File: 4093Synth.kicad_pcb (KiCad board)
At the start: 2 copper layers, 13 parts, among them U1 HEF4093B

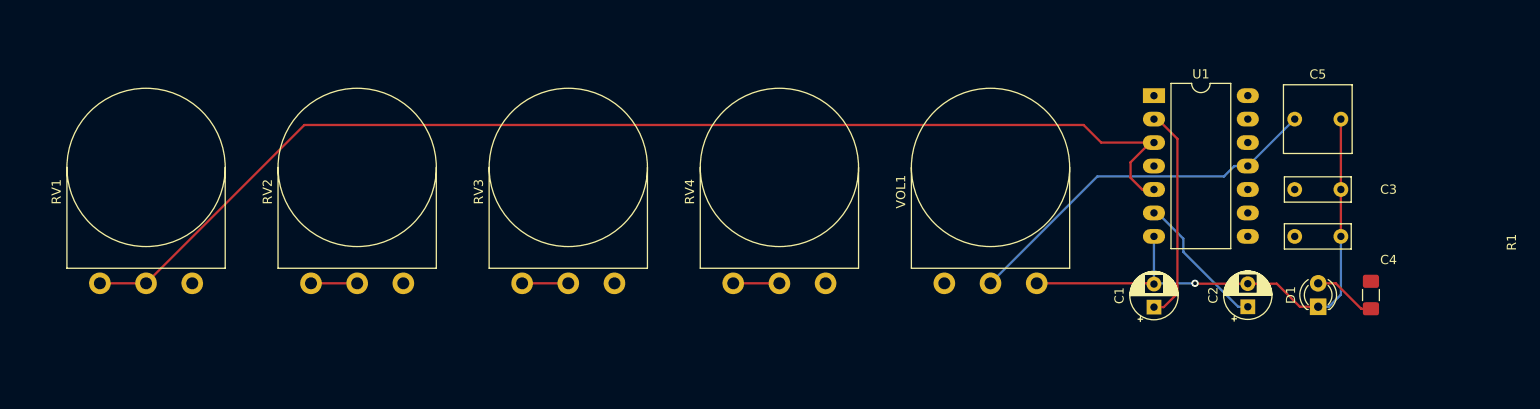
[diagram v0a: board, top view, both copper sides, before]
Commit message: Adds CV in for each Pot
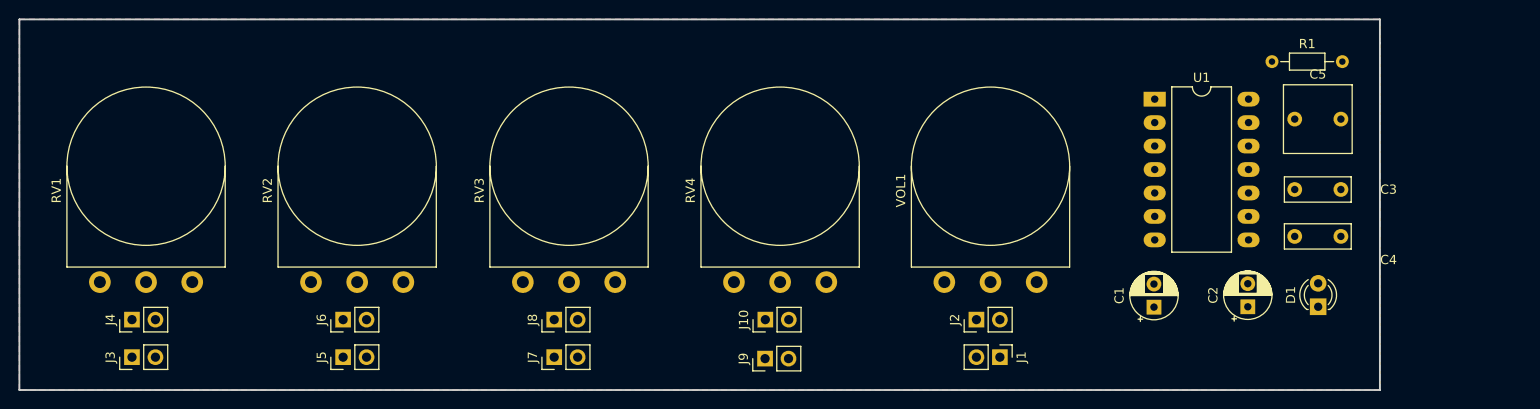
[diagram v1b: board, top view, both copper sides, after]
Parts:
- added J1: Conn_01x02_Female, Connector_PinHeader_2.54mm:PinHeader_1x02_P2.54mm_Vertical, F.Cu at (156.0, 117.2)
- added J10: Conn_01x02_Female, Connector_PinHeader_2.54mm:PinHeader_1x02_P2.54mm_Vertical, F.Cu at (130.6, 113.2)
- added J2: Conn_01x02_Female, Connector_PinHeader_2.54mm:PinHeader_1x02_P2.54mm_Vertical, F.Cu at (153.5, 113.2)
- added J3: Conn_01x02_Female, Connector_PinHeader_2.54mm:PinHeader_1x02_P2.54mm_Vertical, F.Cu at (62.1, 117.2)
- added J4: Conn_01x02_Female, Connector_PinHeader_2.54mm:PinHeader_1x02_P2.54mm_Vertical, F.Cu at (62.1, 113.2)
- added J5: Conn_01x02_Female, Connector_PinHeader_2.54mm:PinHeader_1x02_P2.54mm_Vertical, F.Cu at (84.9, 117.2)
- added J6: Conn_01x02_Female, Connector_PinHeader_2.54mm:PinHeader_1x02_P2.54mm_Vertical, F.Cu at (84.9, 113.2)
- added J7: Conn_01x02_Female, Connector_PinHeader_2.54mm:PinHeader_1x02_P2.54mm_Vertical, F.Cu at (107.8, 117.2)
- added J8: Conn_01x02_Female, Connector_PinHeader_2.54mm:PinHeader_1x02_P2.54mm_Vertical, F.Cu at (107.8, 113.2)
- added J9: Conn_01x02_Female, Connector_PinHeader_2.54mm:PinHeader_1x02_P2.54mm_Vertical, F.Cu at (130.6, 117.4)
- R1: footprint Resistor_SMD:R_1206_3216Metric_Pad1.42x1.75mm_HandSolder -> Resistor_THT:R_Axial_DIN0204_L3.6mm_D1.6mm_P7.62mm_Horizontal
- moved R1 27.5 mm to (185.5, 85.2), turned to 0 degrees
- moved U1 0.39 mm to (172.8, 89.3)
- moved RV3 0.15 mm to (114.4, 109.1)
- moved RV4 0.15 mm to (137.2, 109.1)
- moved RV1 0.13 mm to (68.6, 109.1)
- moved RV2 0.13 mm to (91.4, 109.1)
- moved VOL1 0.13 mm to (160.0, 109.1)
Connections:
- RV1 pad 1: Net-(C1-Pad1) -> Net-(J4-Pad2)
- RV1 pad 2: Net-(RV1-Pad2) -> Net-(J4-Pad1)
- RV1 pad 3: Net-(RV1-Pad2) -> Net-(J4-Pad1)
- RV2 pad 1: Net-(C2-Pad1) -> Net-(J6-Pad2)
- RV2 pad 2: Net-(RV2-Pad2) -> Net-(J6-Pad1)
- RV2 pad 3: Net-(RV2-Pad2) -> Net-(J6-Pad1)
- RV3 pad 1: Net-(C3-Pad1) -> Net-(J8-Pad2)
- RV3 pad 2: Net-(RV3-Pad2) -> Net-(J8-Pad1)
- RV3 pad 3: Net-(RV3-Pad2) -> Net-(J8-Pad1)
- RV4 pad 1: Net-(C4-Pad1) -> Net-(J10-Pad2)
- RV4 pad 2: Net-(C5-Pad1) -> Net-(J10-Pad1)
- RV4 pad 3: Net-(C5-Pad1) -> Net-(J10-Pad1)
- U1 pad 1: Net-(SWT2-Pad1) -> Net-(J1-Pad1)
- U1 pad 10: Net-(RV3-Pad2) -> Net-(J7-Pad1)
- U1 pad 12: Net-(RV3-Pad2) -> Net-(J7-Pad1)
- U1 pad 14: +5V -> Net-(J1-Pad1)
- U1 pad 3: Net-(RV1-Pad2) -> Net-(J3-Pad1)
- U1 pad 4: Net-(RV2-Pad2) -> Net-(J5-Pad1)
- U1 pad 5: Net-(RV1-Pad2) -> Net-(J3-Pad1)
- U1 pad 8: Net-(RV2-Pad2) -> Net-(J5-Pad1)
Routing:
- net Net-(RV1-Pad2): track 130.2 -> 0.00 mm
- net GND: track 58.8 -> 0.00 mm, vias 1 -> 0
- net Net-(C5-Pad1): track 45.3 -> 0.00 mm
- net Net-(C1-Pad1): track 23.3 -> 0.00 mm
- net Net-(C2-Pad1): track 15.2 -> 0.00 mm
- net Net-(D1-Pad2): track 6.86 -> 0.00 mm
- net Net-(RV3-Pad2): track 5.00 -> 0.00 mm
- net Net-(RV2-Pad2): track 5.00 -> 0.00 mm
- added copper zone on F.Cu, net +5V
- added copper zone on B.Cu, net GND
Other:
- board outline added: 147.3 x 40.1 mm
- net class Default: clearance 0.2 -> 0.3; trace_width 0.25 -> 0.5
- rule trace_clearance: 0.2 -> 0.3
